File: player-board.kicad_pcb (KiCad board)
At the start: 2 copper layers, 45 x 30 mm, 23 parts, among them J1 Conn_02x03_Odd_Even, J2 Conn_01x05, U1 AMS1117, U2 ESP32-PICO-D4

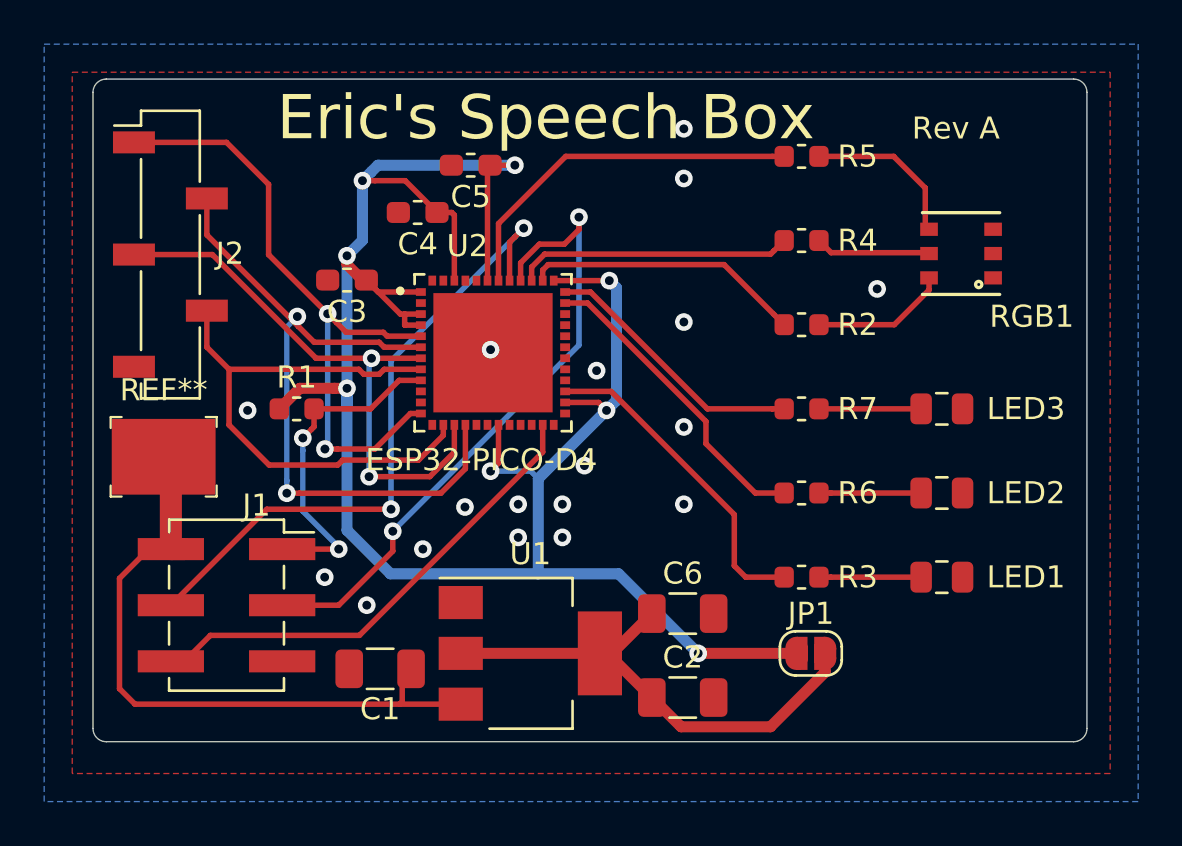
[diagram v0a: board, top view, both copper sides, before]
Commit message: Adding cap on EN.
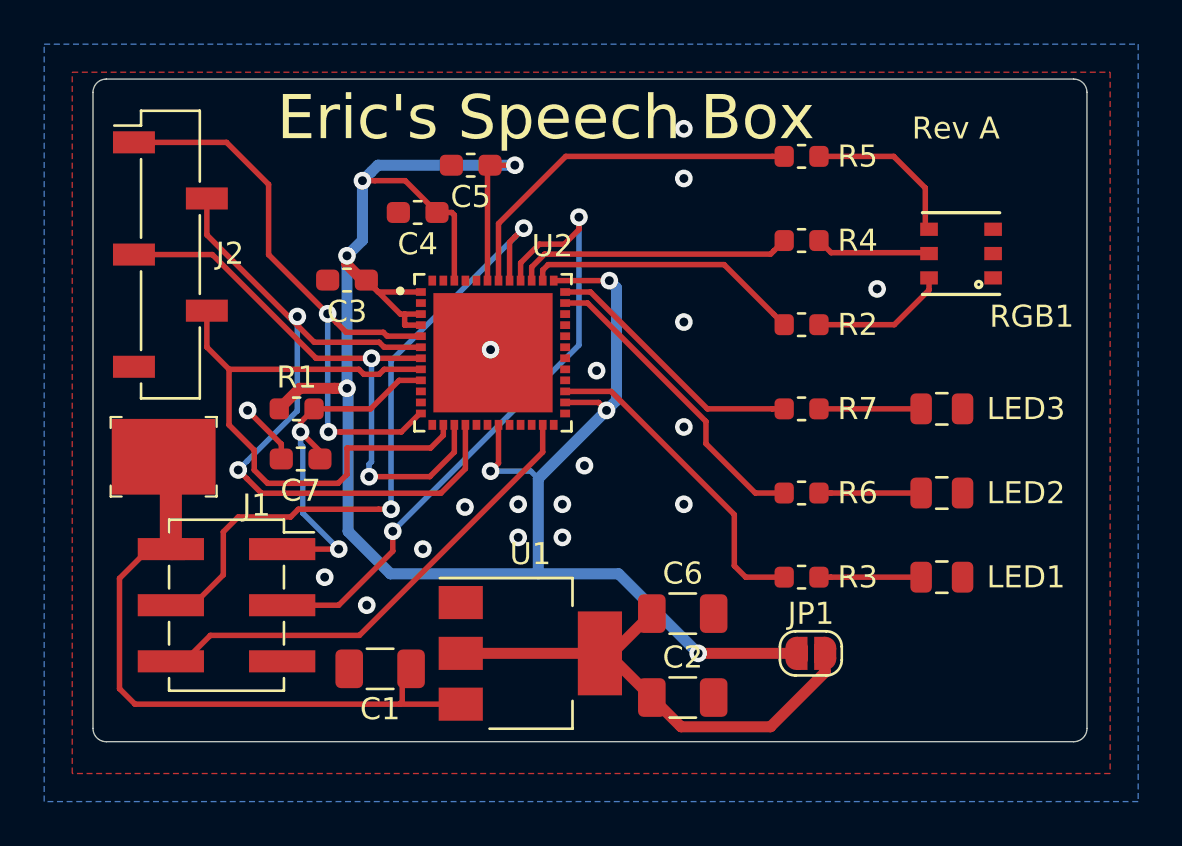
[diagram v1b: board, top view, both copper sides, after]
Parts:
- added C7: 0.1uF, Capacitor_SMD:C_0603_1608Metric_Pad1.05x0.95mm_HandSolder, F.Cu at (109.4, 77.2)
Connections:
- U2 pad 10: (no net) -> Net-(U2-Pad10)
- U2 pad 11: (no net) -> Net-(U2-Pad11)
- U2 pad 13: (no net) -> Net-(U2-Pad13)
- U2 pad 17: (no net) -> Net-(U2-Pad17)
- U2 pad 18: (no net) -> Net-(U2-Pad18)
- U2 pad 2: (no net) -> Net-(U2-Pad2)
- U2 pad 20: (no net) -> Net-(U2-Pad20)
- U2 pad 21: (no net) -> Net-(U2-Pad21)
- U2 pad 22: (no net) -> Net-(U2-Pad22)
- U2 pad 24: (no net) -> Net-(U2-Pad24)
- U2 pad 25: (no net) -> Net-(U2-Pad25)
- U2 pad 28: (no net) -> Net-(U2-Pad28)
- U2 pad 29: (no net) -> Net-(U2-Pad29)
- U2 pad 30: (no net) -> Net-(U2-Pad30)
- U2 pad 31: (no net) -> Net-(U2-Pad31)
- U2 pad 32: (no net) -> Net-(U2-Pad32)
- U2 pad 33: (no net) -> Net-(U2-Pad33)
- U2 pad 34: (no net) -> Net-(U2-Pad34)
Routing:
- net GND: track 0.00 -> 2.83 mm
- net Net-(J2-Pad2): track 32.6 -> 35.1 mm
- net Net-(J2-Pad4): track 25.9 -> 27.9 mm
- net EN: track 15.2 -> 16.8 mm
- net Net-(J2-Pad1): track 29.7 -> 28.4 mm
- net TXD: track 29.6 -> 30.8 mm
- net +3V3: track 96.9 -> 96.2 mm
